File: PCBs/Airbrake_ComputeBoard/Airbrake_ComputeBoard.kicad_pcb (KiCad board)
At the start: 2 copper layers, 9 parts, among them J1 Conn_01x24_Socket, J2 Conn_01x24_Socket

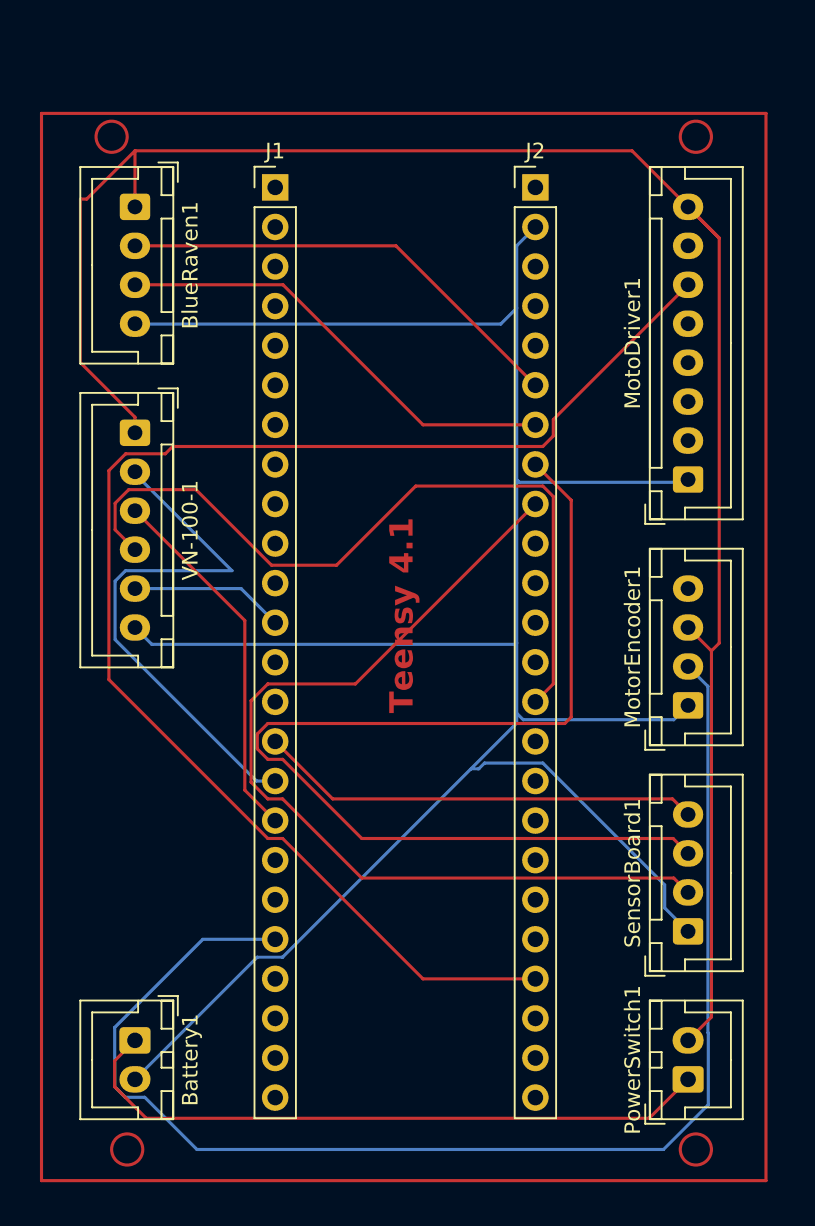
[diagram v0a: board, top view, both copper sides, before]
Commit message: created pcb footprint
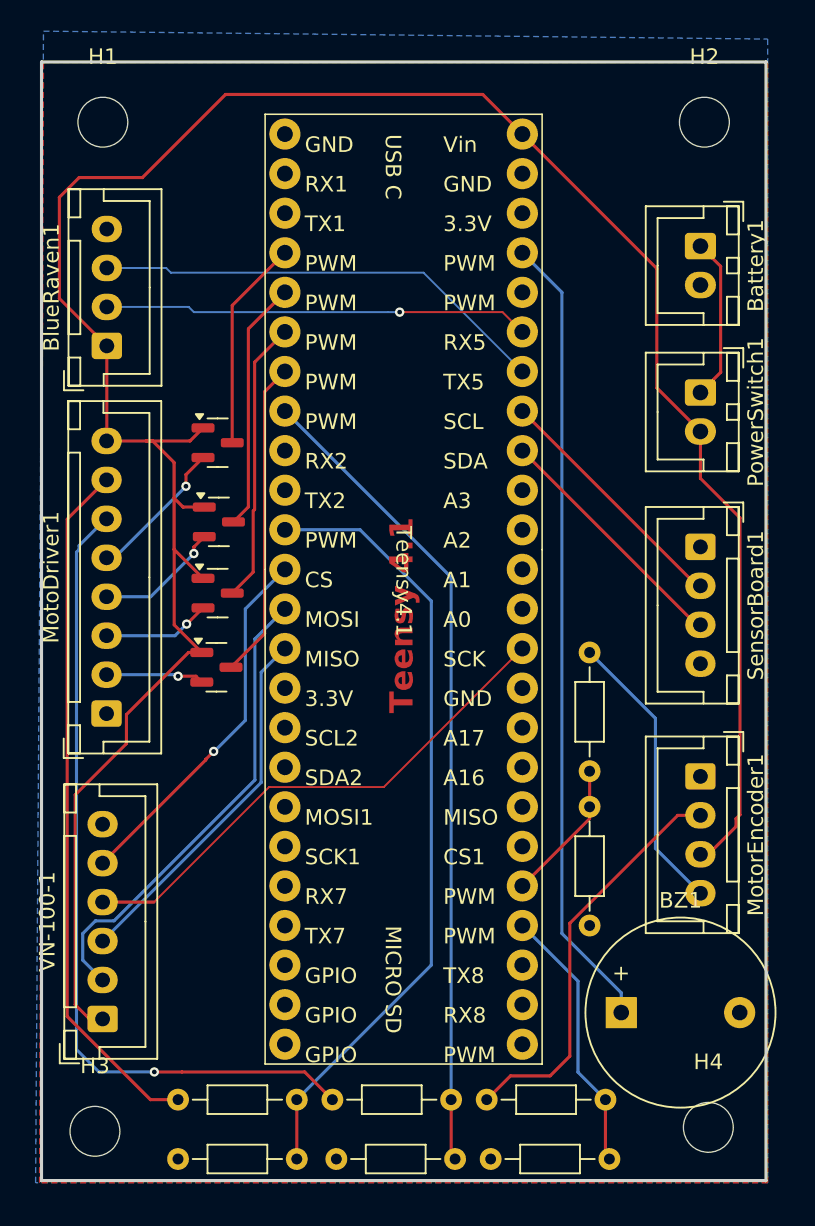
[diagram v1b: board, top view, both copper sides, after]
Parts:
- removed J1, J2: Conn_01x24_Socket, Connector_PinHeader_2.54mm:PinHeader_1x24_P2.54mm_Vertical
- added BZ1: Buzzer, Buzzer_Beeper:Buzzer_12x9.5RM7.6, F.Cu at (172.2, 124.7)
- added H1: MountingHole, MountingHole:MountingHole_3.2mm_M3, F.Cu at (138.9, 67.6)
- added H2: MountingHole, MountingHole:MountingHole_3.2mm_M3, F.Cu at (177.5, 67.6)
- added H3: MountingHole, MountingHole:MountingHole_3.2mm_M3, F.Cu at (138.4, 132.3)
- added H4: MountingHole, MountingHole:MountingHole_3.2mm_M3, F.Cu at (177.8, 132.1)
- added Q1: PNP, Package_TO_SOT_SMD:SOT-23, F.Cu at (146.2, 102.5)
- added Q2: PNP, Package_TO_SOT_SMD:SOT-23, F.Cu at (146.3, 97.8)
- added Q3: PNP, Package_TO_SOT_SMD:SOT-23, F.Cu at (146.4, 93.2)
- added Q4: PNP, Package_TO_SOT_SMD:SOT-23, F.Cu at (146.3, 88.1)
- added R1: 1.7 kOhm, Resistor_THT:R_Axial_DIN0204_L3.6mm_D1.6mm_P7.62mm_Horizontal, F.Cu at (143.8, 130.3)
- added R2: 3.3 kOhm, Resistor_THT:R_Axial_DIN0204_L3.6mm_D1.6mm_P7.62mm_Horizontal, F.Cu at (151.4, 134.1)
- added R3: 1.7 kOhm, Resistor_THT:R_Axial_DIN0204_L3.6mm_D1.6mm_P7.62mm_Horizontal, F.Cu at (153.7, 130.3)
- added R4: 3.3 kOhm, Resistor_THT:R_Axial_DIN0204_L3.6mm_D1.6mm_P7.62mm_Horizontal, F.Cu at (161.5, 134.1)
- added R5: 1.7 kOhm, Resistor_THT:R_Axial_DIN0204_L3.6mm_D1.6mm_P7.62mm_Horizontal, F.Cu at (163.6, 130.3)
- added R6: 3.3 kOhm, Resistor_THT:R_Axial_DIN0204_L3.6mm_D1.6mm_P7.62mm_Horizontal, F.Cu at (171.4, 134.1)
- added R7: 1.7 kOhm, Resistor_THT:R_Axial_DIN0204_L3.6mm_D1.6mm_P7.62mm_Horizontal, F.Cu at (170.2, 101.6)
- added R8: 3.3 kOhm, Resistor_THT:R_Axial_DIN0204_L3.6mm_D1.6mm_P7.62mm_Horizontal, F.Cu at (170.2, 111.5)
- added Teensy4.1: ~, Breakout Boards:Teensy_4.1, F.Cu at (158.2, 97.5)
- moved Battery1 62.6 mm to (177.3, 75.5)
- moved PowerSwitch1 44.1 mm to (177.3, 84.9), turned to -90 degrees
- moved MotoDriver1 40.2 mm to (139.2, 105.5)
- moved VN-100-1 37.7 mm to (138.9, 125.1), turned to 90 degrees
- moved SensorBoard1 24.7 mm to (177.3, 94.8), turned to -90 degrees
- moved BlueRaven1 9.10 mm to (139.2, 81.9), turned to 90 degrees
- moved MotorEncoder1 4.62 mm to (177.3, 109.6), turned to -90 degrees
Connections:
- net +5V renamed Net-(Battery1-Pin_1)
- net Net-(BlueRaven1-Pin_1) renamed /5v_switch
- BlueRaven1 pad 2: Net-(BlueRaven1-Pin_2) -> /BR-TX
- BlueRaven1 pad 3: Net-(BlueRaven1-Pin_3) -> /BR-RX
- MotoDriver1 pad 6: Net-(J2-Pin_21) -> /PG_5v
- MotoDriver1 pad 7: Net-(J2-Pin_24) -> /ALM_5v
- MotorEncoder1 pad 2: Net-(J1-Pin_20) -> /A_5v
- MotorEncoder1 pad 4: Net-(J1-Pin_21) -> /B_5v
- SensorBoard1 pad 2: Net-(J2-Pin_9) -> /SCL
- SensorBoard1 pad 3: Net-(J2-Pin_8) -> /SDA
- SensorBoard1 pad 4: Net-(J1-Pin_15) -> +3.3V
- VN-100-1 pad 2: Net-(J1-Pin_16) -> /MOSI
- VN-100-1 pad 3: Net-(J1-Pin_17) -> /MISO
- VN-100-1 pad 4: Net-(J2-Pin_14) -> /SCK
- VN-100-1 pad 5: Net-(J1-Pin_12) -> /CS
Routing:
- net GND: track 158.4 -> 0.00 mm
- net Net-(J2-Pin_21): track 91.5 -> 0.00 mm
- net Net-(J1-Pin_20): track 86.1 -> 0.00 mm
- net Net-(J2-Pin_8): track 69.2 -> 0.00 mm
- net Net-(J2-Pin_9): track 59.7 -> 0.00 mm
- net /PG_5v: track 0.00 -> 52.6 mm, vias 0 -> 1
- net /PG_3.3v: track 0.00 -> 52.5 mm
- net /buzzer: track 0.00 -> 51.4 mm
- net /ALM_3.3v: track 0.00 -> 50.7 mm
- net Net-(J2-Pin_14): track 50.0 -> 0.00 mm
- net /ALM_5v: track 0.00 -> 44.8 mm
- net /5v_switch: track 121.9 -> 159.0 mm
- net Net-(J1-Pin_16): track 34.5 -> 0.00 mm
- net /SCK: track 0.00 -> 33.7 mm
- net Net-(Battery1-Pin_1): track 42.2 -> 10.5 mm
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- added copper zone on F.Cu, net +3.3V
- added copper zone on B.Cu, net GND
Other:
- board outline added: 46.5 x 71.8 mm

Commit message: created compute board v1.1
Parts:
- removed MotoDriver1: Conn_01x08, Connector_JST:JST_XH_B8B-XH-A_1x08_P2.50mm_Vertical
- removed R3, R5, R7: 1.7 kOhm, Resistor_THT:R_Axial_DIN0204_L3.6mm_D1.6mm_P7.62mm_Horizontal
- removed R4, R6, R8: 3.3 kOhm, Resistor_THT:R_Axial_DIN0204_L3.6mm_D1.6mm_P7.62mm_Horizontal
- added Buck_Converter1: ~, Breakout Boards:Buck_Converter, F.Cu at (142.7, 100.3)
- added MotorDriver1: Conn_01x06, Connector_JST:JST_XH_B6B-XH-A_1x06_P2.50mm_Vertical, F.Cu at (138.9, 86.8)
- BlueRaven1: value Conn_01x04 -> Conn_01x05; footprint Connector_JST:JST_XH_B4B-XH-A_1x04_P2.50mm_Vertical -> Connector_JST:JST_XH_B5B-XH-A_1x05_P2.50mm_Vertical
- R1: value 1.7 kOhm -> 3.3kΩ; footprint Resistor_THT:R_Axial_DIN0204_L3.6mm_D1.6mm_P7.62mm_Horizontal -> Resistor_SMD:R_0805_2012Metric_Pad1.20x1.40mm_HandSolder
- R2: value 3.3 kOhm -> 3.3kΩ; footprint Resistor_THT:R_Axial_DIN0204_L3.6mm_D1.6mm_P7.62mm_Horizontal -> Resistor_SMD:R_0805_2012Metric_Pad1.20x1.40mm_HandSolder
- Teensy4.1: footprint Breakout Boards:Teensy_4.1 -> Breakout Boards:Teensy_4.1_USB
- moved VN-100-1 63.2 mm to (178.1, 75.5), turned to -90 degrees
- moved Battery1 61.9 mm to (139.7, 124.7), turned to 90 degrees
- moved BlueRaven1 52.7 mm to (156.2, 131.8), turned to 180 degrees
- moved PowerSwitch1 48.6 mm to (139.9, 116.1), turned to 90 degrees
- moved R1 34.5 mm to (177.1, 121.4), turned to 180 degrees
- moved R2 26.8 mm to (176.8, 125.5)
- moved BZ1 22.0 mm to (150.4, 122.4), turned to 90 degrees
- moved Q1 16.3 mm to (146.2, 86.3)
- moved Q2 16.3 mm to (146.3, 81.5)
- moved Q3 16.3 mm to (146.4, 77.0)
- moved Q4 16.3 mm to (146.3, 71.9)
- moved MotorEncoder1 14.8 mm to (177.3, 94.8)
- moved SensorBoard1 14.4 mm to (177.5, 109.3)
- moved Teensy4.1 6.91 mm to (164.8, 95.5)
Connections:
- net /EN renamed /Stop
- net /F/R renamed /Dir
- BlueRaven1 pad 1: /5v_switch -> /usb_5v
- BlueRaven1 pad 2: /BR-TX -> /D-
- BlueRaven1 pad 3: /BR-RX -> /D+
- MotorEncoder1 pad 2: /A_5v -> /Encoder_A
- MotorEncoder1 pad 3: /5v_switch -> +5V
- MotorEncoder1 pad 4: /B_5v -> /Encoder_B
- PowerSwitch1 pad 1: Net-(Battery1-Pin_1) -> Net-(Buck_Converter1-VIN)
- PowerSwitch1 pad 2: /5v_switch -> Net-(Battery1-Pin_1)
- Q1 pad 3: /5v_switch -> GND
- Q2 pad 3: /5v_switch -> GND
- Q3 pad 3: /5v_switch -> +5V
- Q4 pad 3: /5v_switch -> +5V
- R1 pad 1: /ALM_5v -> /SCL
- R1 pad 2: /ALM_3.3v -> +3.3V
- R2 pad 1: /ALM_3.3v -> +3.3V
- R2 pad 2: GND -> /SDA
- Teensy4.1 pad 10: /ALM_3.3v -> unconnected-(Teensy4.1-PWM-Pad10)
- Teensy4.1 pad 27: /A_3.3v -> /Encoder_A
- Teensy4.1 pad 28: /B_3.3v -> /Encoder_B
- Teensy4.1 pad 47: /5v_switch -> +5V
- Teensy4.1 pad 7: /PG_3.3v -> unconnected-(Teensy4.1-PWM-Pad7)
- VN-100-1 pad 1: /5v_switch -> +5V
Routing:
- net /5v_switch: track 159.0 -> 0.00 mm
- net +5V: track 0.00 -> 134.6 mm
- net /usb_5v: track 0.00 -> 68.5 mm
- net /D-: track 0.00 -> 67.3 mm
- net /D+: track 0.00 -> 65.6 mm
- net /PG_5v: track 52.6 -> 0.00 mm, vias 1 -> 0
- net /PG_3.3v: track 52.5 -> 0.00 mm
- net /ALM_3.3v: track 50.7 -> 0.00 mm
- net /ALM_5v: track 44.8 -> 0.00 mm
- net /BR-RX: track 29.4 -> 0.00 mm
- net /BR-TX: track 27.3 -> 0.00 mm, vias 1 -> 0
- net /A_5v: track 26.3 -> 0.00 mm
- net /SDA: track 16.1 -> 42.2 mm
- net /SCL: track 16.1 -> 41.8 mm
- net /buzzer: track 51.4 -> 74.8 mm, vias 0 -> 1
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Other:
- board text added: "TRT Airbrake Compute Board v1.1"

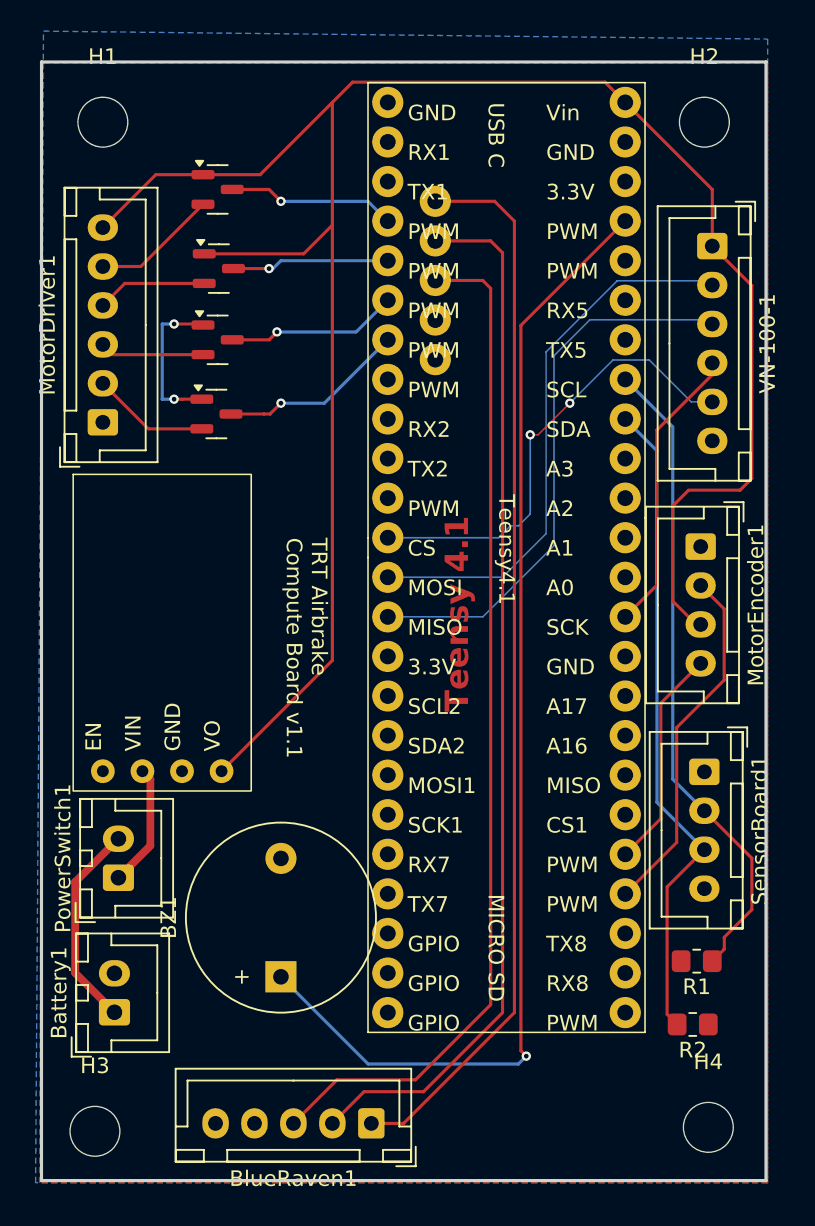
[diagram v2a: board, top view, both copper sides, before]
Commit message: Updated PCB to add resistors to level shifters.
Updated PCB; Added resistors
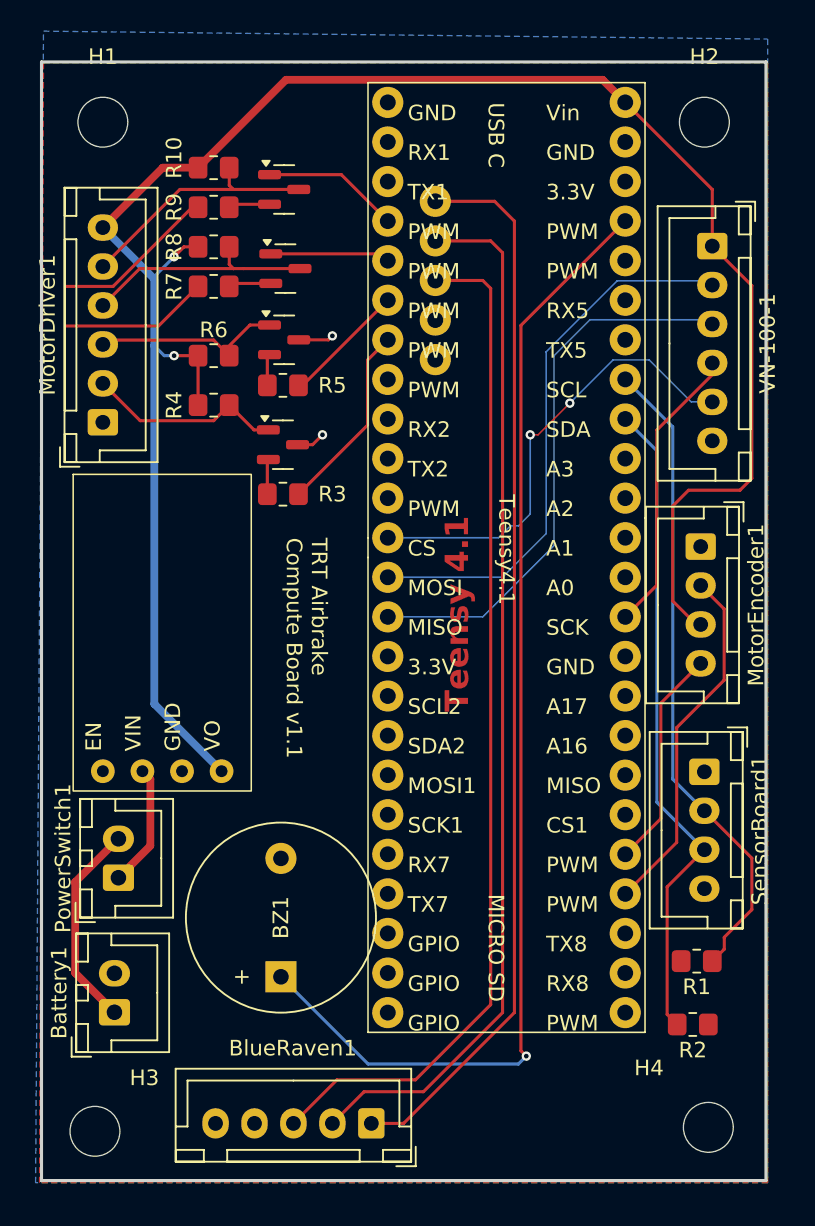
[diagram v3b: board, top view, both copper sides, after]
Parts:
- added R10: 10kΩ, Resistor_SMD:R_0805_2012Metric_Pad1.20x1.40mm_HandSolder, F.Cu at (146.1, 70.5)
- added R3: 10kΩ, Resistor_SMD:R_0805_2012Metric_Pad1.20x1.40mm_HandSolder, F.Cu at (150.5, 91.4)
- added R4: 3.3kΩ, Resistor_SMD:R_0805_2012Metric_Pad1.20x1.40mm_HandSolder, F.Cu at (146.1, 85.7)
- added R5: 10kΩ, Resistor_SMD:R_0805_2012Metric_Pad1.20x1.40mm_HandSolder, F.Cu at (150.5, 84.5)
- added R6: 3.3kΩ, Resistor_SMD:R_0805_2012Metric_Pad1.20x1.40mm_HandSolder, F.Cu at (146.1, 82.5)
- added R7: 3.3kΩ, Resistor_SMD:R_0805_2012Metric_Pad1.20x1.40mm_HandSolder, F.Cu at (146.1, 78.1)
- added R8: 10kΩ, Resistor_SMD:R_0805_2012Metric_Pad1.20x1.40mm_HandSolder, F.Cu at (146.1, 75.6)
- added R9: 3.3kΩ, Resistor_SMD:R_0805_2012Metric_Pad1.20x1.40mm_HandSolder, F.Cu at (146.1, 73.0)
- Q1, Q2, Q3, Q4: value PNP -> Q_NPN_BEC
- moved Q1 4.70 mm to (150.5, 88.3)
- moved Q2 4.27 mm to (150.6, 81.5)
- moved Q3 4.27 mm to (150.7, 77.0)
- moved Q4 4.27 mm to (150.6, 71.9)
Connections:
- Q1 pad 1: Net-(MotorDriver1-Pin_2) -> Net-(Q1-B)
- Q1 pad 2: /Dir -> GND
- Q1 pad 3: GND -> Net-(MotorDriver1-Pin_2)
- Q2 pad 1: Net-(MotorDriver1-Pin_3) -> Net-(Q2-B)
- Q2 pad 2: /Stop -> GND
- Q2 pad 3: GND -> Net-(MotorDriver1-Pin_3)
- Q3 pad 1: Net-(MotorDriver1-Pin_4) -> Net-(Q3-B)
- Q3 pad 2: /BK -> Net-(MotorDriver1-Pin_4)
- Q3 pad 3: +5V -> /BK
- Q4 pad 1: Net-(MotorDriver1-Pin_5) -> Net-(Q4-B)
- Q4 pad 2: /SV -> Net-(MotorDriver1-Pin_5)
- Q4 pad 3: +5V -> /SV
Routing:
- net +3.3V: track 0.00 -> 20.2 mm
- net Net-(MotorDriver1-Pin_4): track 7.09 -> 15.1 mm
- net Net-(MotorDriver1-Pin_5): track 8.08 -> 16.1 mm
- net +5V: track 134.6 -> 127.9 mm, vias 0 -> 2
- net GND: track 10.0 -> 4.13 mm
- net Net-(MotorDriver1-Pin_2): track 7.56 -> 12.7 mm
- net Net-(MotorDriver1-Pin_3): track 6.70 -> 11.8 mm
- net /Stop: track 11.0 -> 7.99 mm, vias 1 -> 0
- net Net-(Q3-B): track 0.00 -> 2.74 mm
- net Net-(Q4-B): track 0.00 -> 2.67 mm
- net /BK: track 10.1 -> 7.69 mm, vias 1 -> 0
- net Net-(Q1-B): track 0.00 -> 2.25 mm
- net Net-(Q2-B): track 0.00 -> 2.03 mm
- net /SV: track 10.8 -> 8.83 mm, vias 1 -> 0
- net /Dir: track 12.0 -> 12.3 mm, vias 1 -> 0

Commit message: Made new PCB
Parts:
- removed Q1, Q2, Q3, Q4: Q_NPN_BEC, Package_TO_SOT_SMD:SOT-23
- removed R10, R8: 10kΩ, Resistor_SMD:R_0805_2012Metric_Pad1.20x1.40mm_HandSolder
- removed R4, R6, R7, R9: 3.3kΩ, Resistor_SMD:R_0805_2012Metric_Pad1.20x1.40mm_HandSolder
- added C1: 0.1µF, Capacitor_SMD:C_0805_2012Metric_Pad1.18x1.45mm_HandSolder, F.Cu at (150.5, 102.9)
- added C2: 0.1µF, Capacitor_SMD:C_0805_2012Metric_Pad1.18x1.45mm_HandSolder, F.Cu at (145.4, 102.9)
- added LimitSwitch1: Conn_01x02, Connector_JST:JST_XH_B2B-XH-A_1x02_P2.50mm_Vertical, F.Cu at (148.0, 67.9)
- added U1: PC817, Package_DIP:DIP-4_W7.62mm, F.Cu at (154.3, 86.4)
- added U2: TXB0104D, Package_SO:SOIC-14_3.9x8.7mm_P1.27mm, F.Cu at (148.0, 95.2)
- added U3: PC817, Package_DIP:DIP-4_W7.62mm, F.Cu at (154.3, 78.1)
- R3, R5: value 10kΩ -> 180Ω
- moved R3 18.7 mm to (153.0, 72.9)
- moved R5 4.07 mm to (153.0, 81.3)
- moved PowerSwitch1 0.24 mm to (139.7, 116.1)
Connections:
- MotorDriver1 pad 2: Net-(MotorDriver1-Pin_2) -> /Dir_5V
- MotorDriver1 pad 3: Net-(MotorDriver1-Pin_3) -> /Stop_5V
- MotorDriver1 pad 4: Net-(MotorDriver1-Pin_4) -> /BK_5V
- MotorDriver1 pad 5: Net-(MotorDriver1-Pin_5) -> /SV_5V
- MotorEncoder1 pad 2: /Encoder_A -> /Encoder_A_5V
- MotorEncoder1 pad 4: /Encoder_B -> /Encoder_B_5V
- R3 pad 1: /Dir -> Net-(R3-Pad1)
- R3 pad 2: Net-(Q1-B) -> GND
- R5 pad 1: /Stop -> Net-(R5-Pad1)
- R5 pad 2: Net-(Q2-B) -> GND
- Teensy4.1 pad 7: unconnected-(Teensy4.1-PWM-Pad7) -> /Limit_Switch
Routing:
- net +3.3V: track 20.2 -> 126.1 mm, vias 0 -> 3
- net GND: track 4.13 -> 51.3 mm, vias 2 -> 0
- net /Encoder_B_5V: track 0.00 -> 35.4 mm, vias 0 -> 1
- net /Encoder_A_5V: track 0.00 -> 34.4 mm, vias 0 -> 1
- net /SV_5V: track 0.00 -> 20.4 mm
- net /Limit_Switch: track 0.00 -> 19.6 mm
- net /BK_5V: track 0.00 -> 19.2 mm
- net Net-(MotorDriver1-Pin_5): track 16.1 -> 0.00 mm
- net /BK: track 7.69 -> 23.5 mm
- net /SV: track 8.83 -> 24.2 mm
- net /Encoder_B: track 14.3 -> 29.5 mm, vias 0 -> 1
- net Net-(MotorDriver1-Pin_4): track 15.1 -> 0.00 mm
- net Net-(MotorDriver1-Pin_2): track 12.7 -> 0.00 mm
- net Net-(MotorDriver1-Pin_3): track 11.8 -> 0.00 mm
- net /Stop_5V: track 0.00 -> 9.28 mm
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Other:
- board text added: "104"
- board text added: "180"
- board text added: "3k3"
- board text added: "5V"
- board text added: "BK"
- board text added: "Dir"
- board text added: "GND"
- board text added: "SV"
- board text added: "Stop"
- board text added: "TRT Airbrake Compute Board v1.2"
- board text removed: "TRT Airbrake Compute Board v1.1"
